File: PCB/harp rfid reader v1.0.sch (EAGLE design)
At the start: 38 parts, among them IC1 FT232RL, IC2 LP5907MFX-3.3, IC3 ATXMEGAxxxA4U-AU, Q1 BC817-40W, U1 ID-12/20SMD

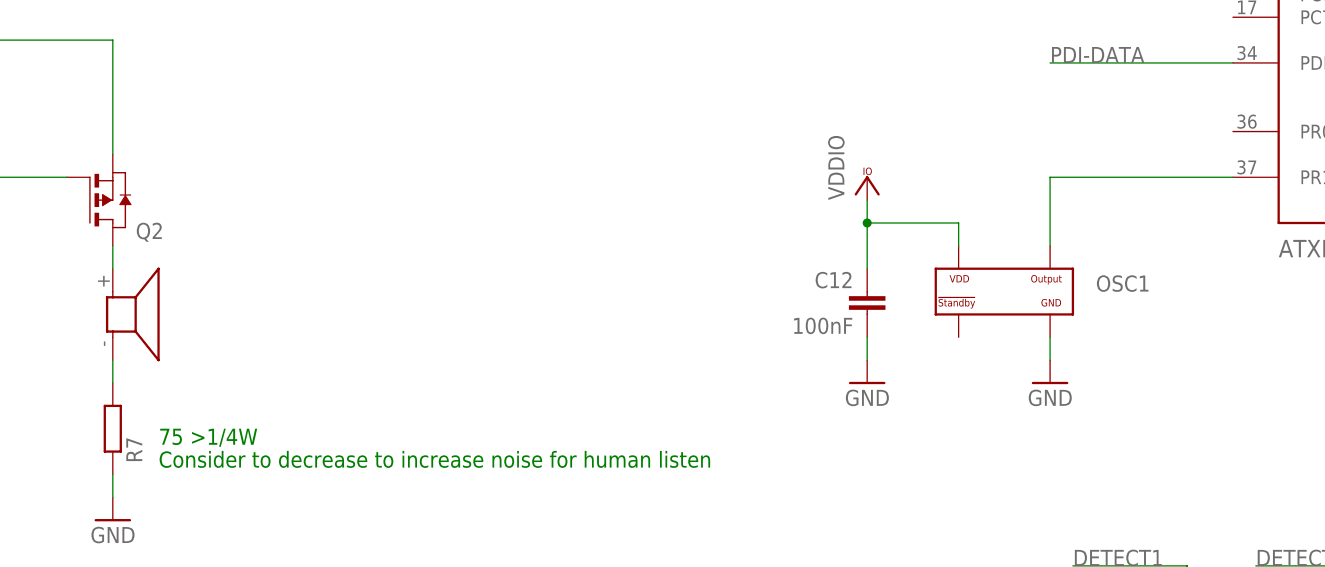
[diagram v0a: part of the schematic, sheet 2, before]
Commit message: Increased oscillator and buzzer pads.
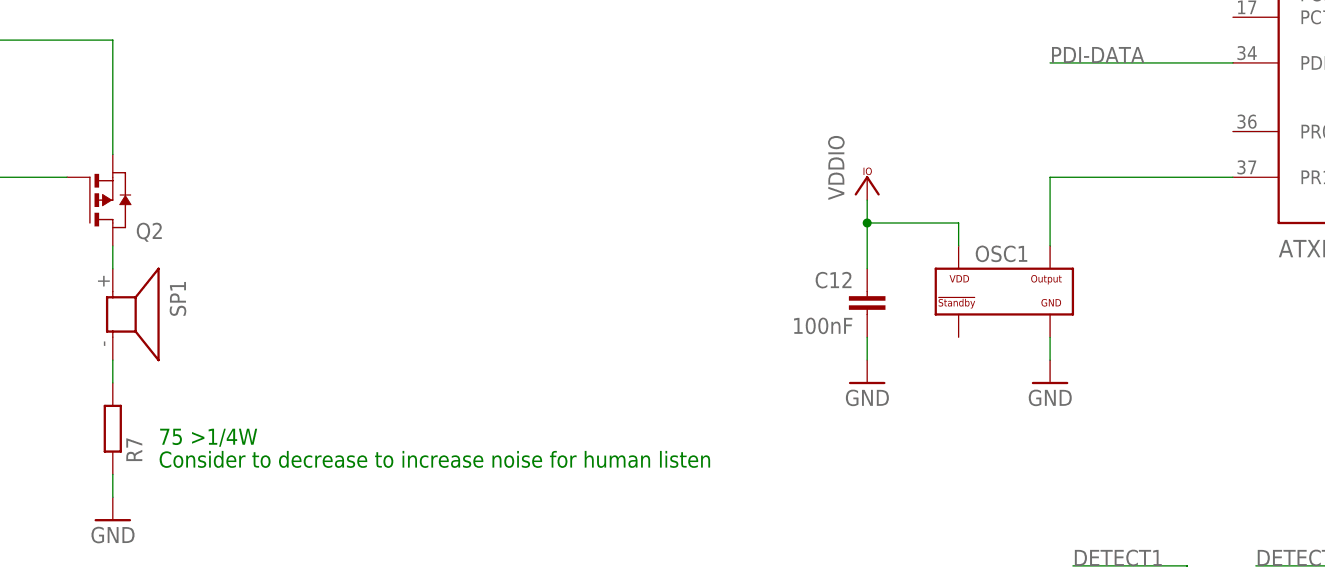
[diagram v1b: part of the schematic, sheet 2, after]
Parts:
- OSC1: value OSCILLATOR -> CNP-MISCELLANEOUS_OSCILLATOR; device CNP-miscellaneous:OSCILLATOR -> harp rfid reader v1.0:CNP-MISCELLANEOUS_OSCILLATOR
- SP1: value SMT-0540-S-R -> BUZZER-COIL_SMT-0540-S-R; device Buzzer Coil:SMT-0540-S-R -> harp rfid reader v1.0:BUZZER-COIL_SMT-0540-S-R
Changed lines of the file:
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@@
 <layer number="59" name="tCarbon" color="7" fill="1" visible="no" active="no"/>
 <layer number="60" name="bCarbon" color="7" fill="1" visible="no" active="no"/>
+<layer number="88" name="SimResults" color="9" fill="1" visible="yes" active="yes"/>
+<layer number="89" name="SimProbes" color="9" fill="1" visible="yes" active="yes"/>
 <layer number="90" name="Modules" color="7" fill="1" visible="yes" active="yes"/>
 <layer number="91" name="Nets" color="2" fill="1" visible="yes" active="yes"/>
@@
 <part name="R1" library="rcl" deviceset="R-EU_" device="R0402" value="1M"/>
 <part name="VCC12" library="supply1" deviceset="VCCIO" device="" value="VDDIO"/>
-<part name="OSC1" library="CNP-miscellaneous" deviceset="OSCILLATOR" device="" value=""/>
 <part name="GND59" library="supply1" deviceset="GND" device=""/>
 <part name="C12" library="rcl" deviceset="C-EU" device="C0402" value="100nF"/>
@@
 <part name="GND5" library="SparkFun" deviceset="GND" device=""/>
 <part name="GND6" library="SparkFun" deviceset="GND" device=""/>
-<part name="SP1" library="Buzzer Coil" deviceset="SMT-0540-S-R" device=""/>
 <part name="R7" library="rcl" deviceset="R-EU_" device="R0402" value="75 &gt;1/4W"/>
 <part name="STATE" library="led" library_urn="urn:adsk.eagle:library:259" deviceset="LED" device="CHIP-LED0603" package3d_urn="urn:adsk.eagle:package:15819/3"/>
@@
 <part name="GND10" library="supply1" deviceset="GND" device=""/>
 <part name="VCC1" library="supply1" deviceset="VCCIO" device="" value="VDDIO"/>
+<part name="OSC1" library="harp rfid reader v1.0" deviceset="CNP-MISCELLANEOUS_OSCILLATOR" device=""/>
+<part name="SP1" library="harp rfid reader v1.0" deviceset="BUZZER-COIL_SMT-0540-S-R" device=""/>
 </parts>
 <sheets>
@@
 <attribute name="SHEET" x="357.505" y="5.08" size="2.54" layer="94" font="vector"/>
 </instance>
-<instance part="OSC1" gate="G$1" x="172.72" y="116.84" smashed="yes">
-<attribute name="VALUE" x="182.88" y="114.3" size="1.778" layer="96"/>
-<attribute name="NAME" x="182.88" y="116.84" size="1.778" layer="95"/>
-</instance>
 <instance part="GND59" gate="1" x="177.8" y="106.68" smashed="yes" rot="MR0">
 <attribute name="VALUE" x="180.34" y="104.14" size="1.778" layer="96" rot="MR0"/>
@@
 <attribute name="VALUE" x="157.48" y="180.34" size="1.778" layer="96"/>
 </instance>
-<instance part="SP1" gate="G$1" x="73.66" y="114.3" smashed="yes" rot="R270"/>
 <instance part="R7" gate="G$1" x="73.66" y="101.6" smashed="yes" rot="MR90">
 <attribute name="NAME" x="75.1586" y="97.79" size="1.778" layer="95" rot="MR90"/>
@@
 <instance part="VCC1" gate="G$1" x="96.52" y="185.42" smashed="yes">
 <attribute name="VALUE" x="93.98" y="182.88" size="1.778" layer="96" rot="R90"/>
+</instance>
+<instance part="OSC1" gate="G$1" x="172.72" y="116.84" smashed="yes">
+<attribute name="NAME" x="169.418" y="120.142" size="1.778" layer="95"/>
+</instance>
+<instance part="SP1" gate="G$1" x="73.66" y="114.3" smashed="yes" rot="R270">
+<attribute name="NAME" x="80.01" y="118.11" size="1.778" layer="95" rot="R270"/>
 </instance>
 </instances>
@@
 </segment>
 <segment>
-<pinref part="OSC1" gate="G$1" pin="VDD"/>
 <wire x1="167.64" y1="121.92" x2="167.64" y2="124.46" width="0.1524" layer="91"/>
 <wire x1="167.64" y1="124.46" x2="157.48" y2="124.46" width="0.1524" layer="91"/>
@@
 <junction x="157.48" y="124.46"/>
 <pinref part="VCC10" gate="G$1" pin="VCCIO"/>
+<pinref part="OSC1" gate="G$1" pin="VDD"/>
 </segment>
 <segment>
@@
 <net name="GND" class="0">
 <segment>
-<pinref part="OSC1" gate="G$1" pin="GND"/>
 <pinref part="GND59" gate="1" pin="GND"/>
 <wire x1="177.8" y1="109.22" x2="177.8" y2="111.76" width="0.1524" layer="91"/>
+<pinref part="OSC1" gate="G$1" pin="GND"/>
 </segment>
 <segment>
@@
 <net name="OSC1" class="0">
 <segment>
-<pinref part="OSC1" gate="G$1" pin="OUTPUT"/>
 <wire x1="177.8" y1="121.92" x2="177.8" y2="129.54" width="0.1524" layer="91"/>
 <pinref part="IC3" gate="G$1" pin="PR1/XTAL1"/>
 <wire x1="177.8" y1="129.54" x2="198.12" y2="129.54" width="0.1524" layer="91"/>
+<pinref part="OSC1" gate="G$1" pin="OUTPUT"/>
 </segment>
 </net>
@@
 <segment>
 <pinref part="R7" gate="G$1" pin="2"/>
+<wire x1="73.66" y1="106.68" x2="73.66" y2="109.22" width="0.1524" layer="91"/>
 <pinref part="SP1" gate="G$1" pin="-"/>
-<wire x1="73.66" y1="106.68" x2="73.66" y2="109.22" width="0.1524" layer="91"/>
 </segment>
 </net>
@@
 <segment>
 <pinref part="Q2" gate="G$1" pin="D"/>
+<wire x1="73.66" y1="121.92" x2="73.66" y2="119.38" width="0.1524" layer="91"/>
 <pinref part="SP1" gate="G$1" pin="+"/>
-<wire x1="73.66" y1="121.92" x2="73.66" y2="119.38" width="0.1524" layer="91"/>
-</segment>
-</net>
+</segment>
+</net>
